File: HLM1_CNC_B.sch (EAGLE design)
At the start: 19 parts, among them Q1 600mA/40V, Q2 IRF540

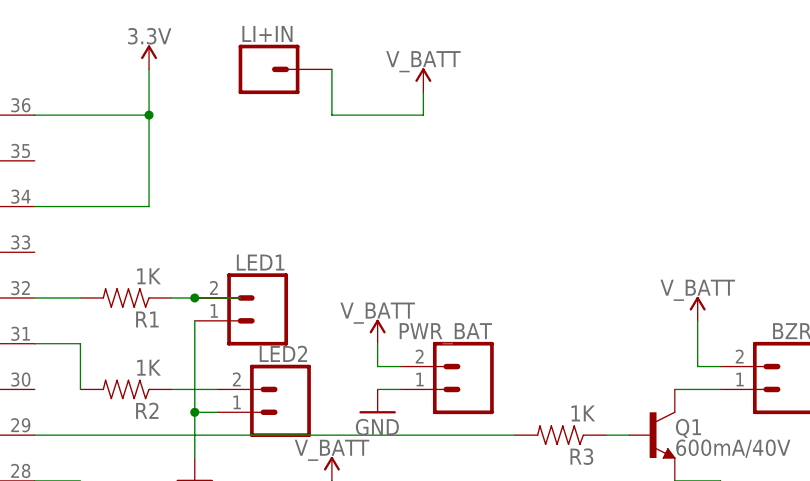
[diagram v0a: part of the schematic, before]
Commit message: Improved naming and file structure
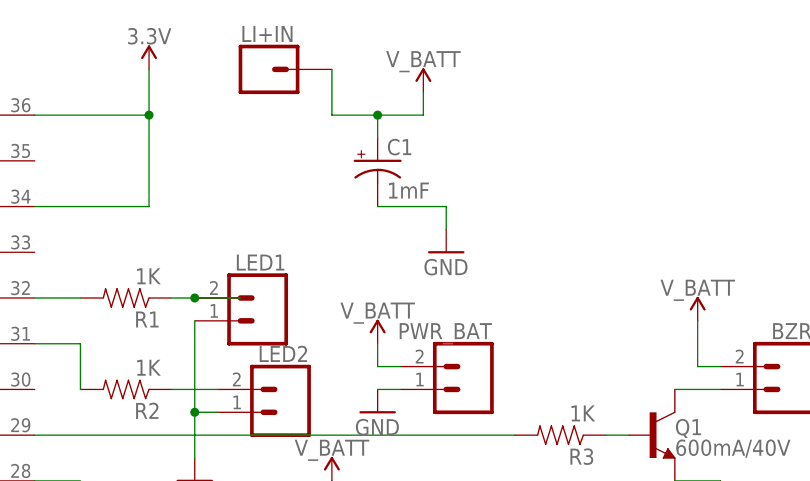
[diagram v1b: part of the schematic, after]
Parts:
- added C1: 1mF, SparkFun-Capacitors:1000UF-RADIAL-5MM-25V-20%
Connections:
- net GND: now also C1.-
- net V_BATT: now also C1.+
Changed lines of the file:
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@@
 <part name="LED2" library="SparkFun-Connectors" deviceset="CONN_02" device=""/>
 <part name="R2" library="SparkFun-Passives" deviceset="RESISTOR" device="PTH-1/6W" value="1K"/>
+<part name="C1" library="SparkFun-Capacitors" deviceset="1000UF" device="-RADIAL-5MM-25V-20%" value="1mF"/>
+<part name="GND10" library="supply1" library_urn="urn:adsk.eagle:library:371" deviceset="GND" device=""/>
 </parts>
 <sheets>
@@
 <instance part="LED2" gate="G$1" x="104.14" y="58.42" rot="MR0"/>
 <instance part="R2" gate="G$1" x="86.36" y="60.96" rot="R180"/>
+<instance part="C1" gate="G$1" x="114.3" y="86.36"/>
+<instance part="GND10" gate="1" x="121.92" y="76.2"/>
 </instances>
 <busses>
@@
 <pinref part="LI+IN" gate="G$1" pin="1"/>
 <wire x1="109.22" y1="96.52" x2="109.22" y2="91.44" width="0.1524" layer="91"/>
-<wire x1="119.38" y1="91.44" x2="109.22" y2="91.44" width="0.1524" layer="91"/>
+<wire x1="119.38" y1="91.44" x2="114.3" y2="91.44" width="0.1524" layer="91"/>
+<pinref part="C1" gate="G$1" pin="+"/>
+<wire x1="114.3" y1="91.44" x2="109.22" y2="91.44" width="0.1524" layer="91"/>
+<wire x1="114.3" y1="91.44" x2="114.3" y2="88.9" width="0.1524" layer="91"/>
+<junction x="114.3" y="91.44"/>
 </segment>
 <segment>
@@
 <junction x="93.98" y="58.42"/>
 </segment>
-</net>
+<segment>
+<pinref part="C1" gate="G$1" pin="-"/>
+<wire x1="114.3" y1="81.28" x2="121.92" y2="81.28" width="0.1524" layer="91"/>
+<wire x1="121.92" y1="81.28" x2="121.92" y2="78.74" width="0.1524" layer="91"/>
+<pinref part="GND10" gate="1" pin="GND"/>
+</segment>
+</net>
